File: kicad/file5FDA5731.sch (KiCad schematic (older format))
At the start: 14 parts, among them M1 BSC014N04LSI, M11 BSC014N04LSI, M12 BSC010N04LSI, M13 BSC015NE2LS5I, M14 BSC009NE2LS5I, M15 BSC014N04LSI, M17 BSC015NE2LS5I, M2 BSC010N04LSI, M3 BSC015NE2LS5I, M4 BSC009NE2LS5I, M5 BSC014N04LSI, M7 BSC015NE2LS5I

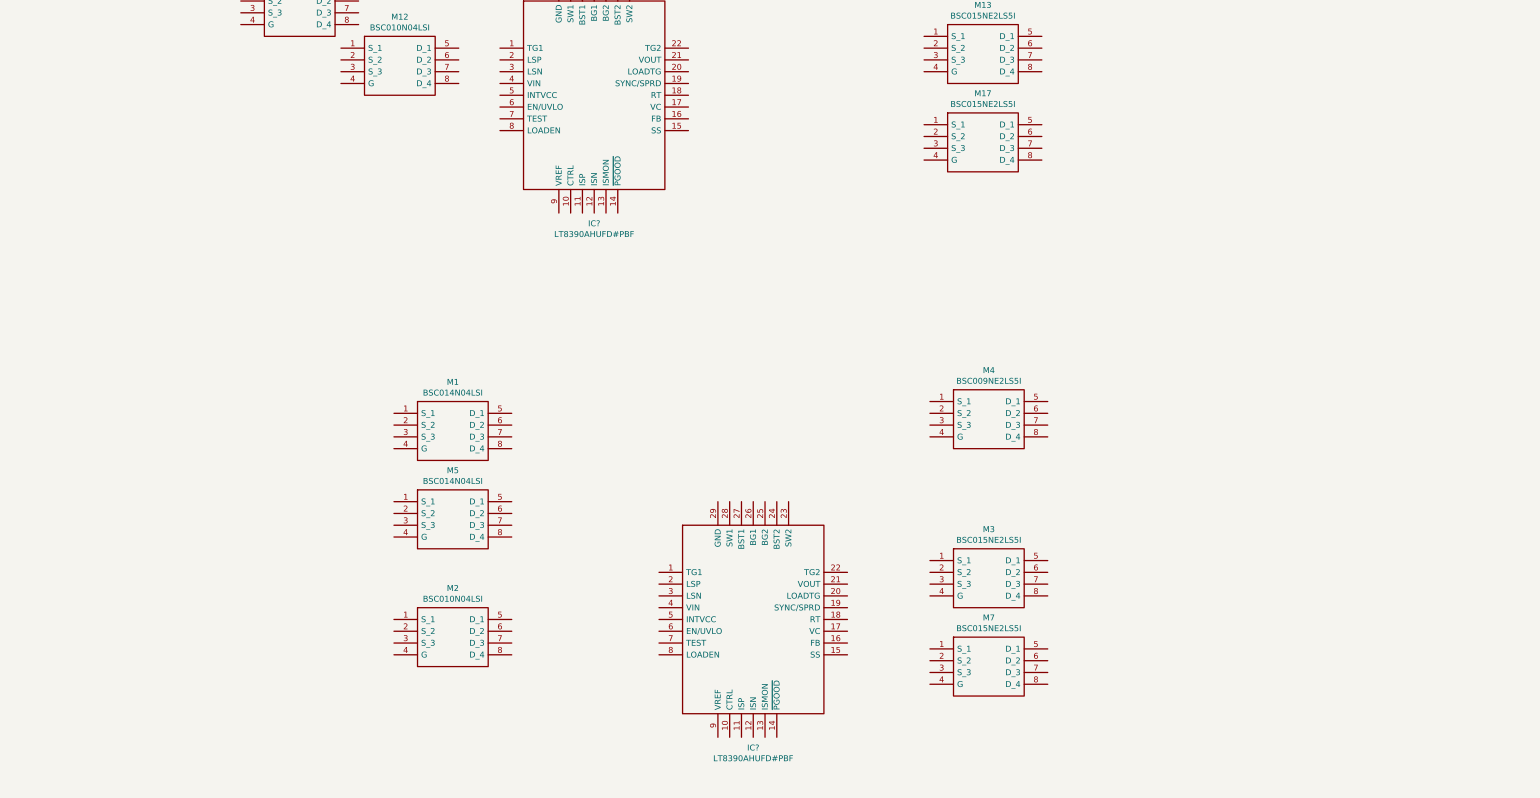
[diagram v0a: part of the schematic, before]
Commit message: Add Vin
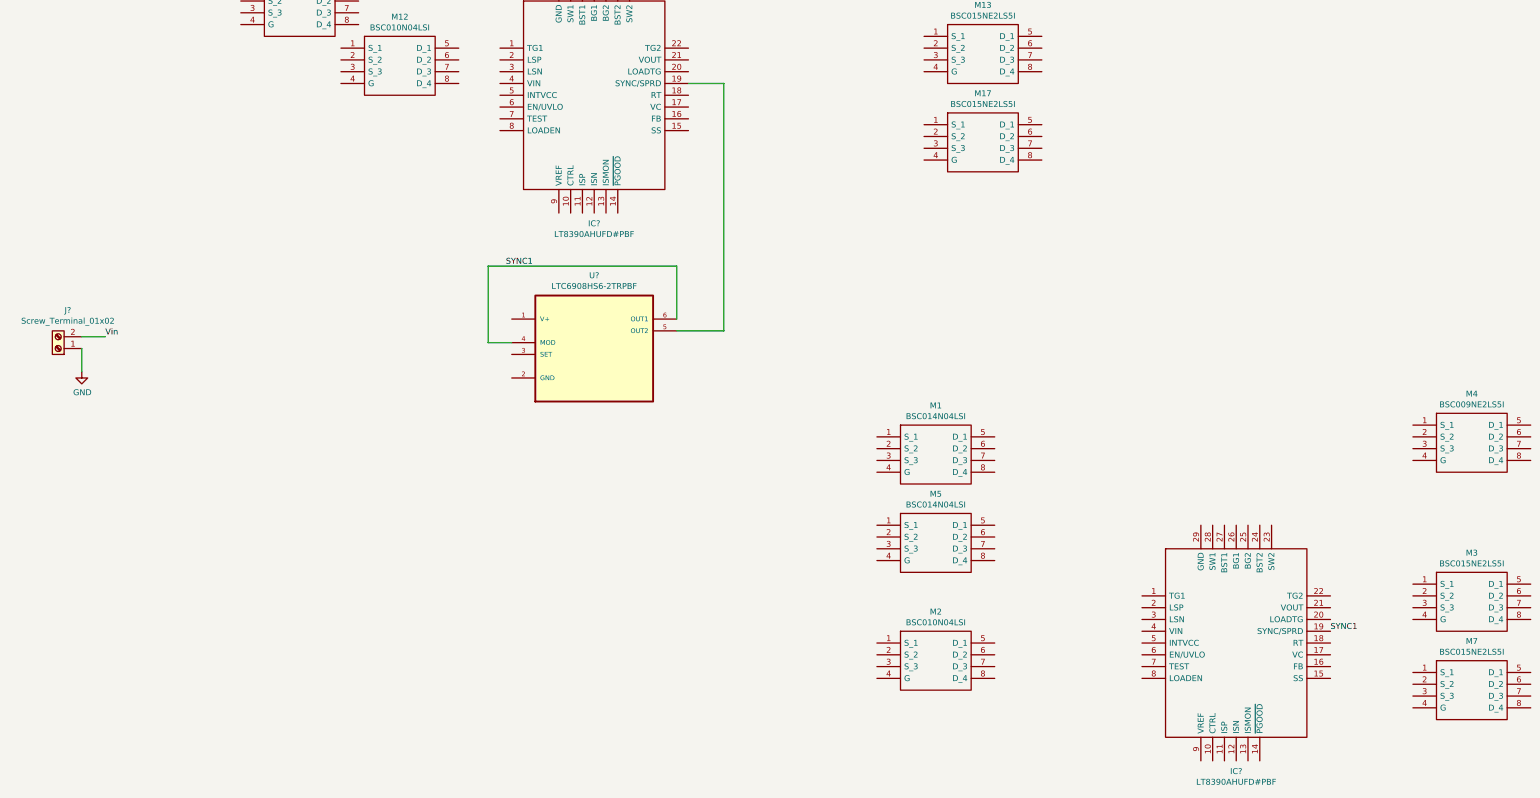
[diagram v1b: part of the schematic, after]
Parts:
- added J?: Screw_Terminal_01x02, symbol Connector:Screw_Terminal_01x02
- added U?: LTC6908HS6-2TRPBF, SOT95P280X100-6N, symbol LTC6908HS6-2TRPBF:LTC6908HS6-2TRPBF
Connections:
- net at IC?.19 (SYNC/SPRD): now also U?.5 (OUT2)
- net SYNC1: now reaches IC?.19 (SYNC/SPRD)
- net SYNC1: now also U?.4 (MOD), U?.6 (OUT1)
- new net GND: J?.1 (Pin_1)
- new net Vin: J?.2 (Pin_2)
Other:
- moved on the sheet: IC?, M1, M2, M3, M4, M5, M7

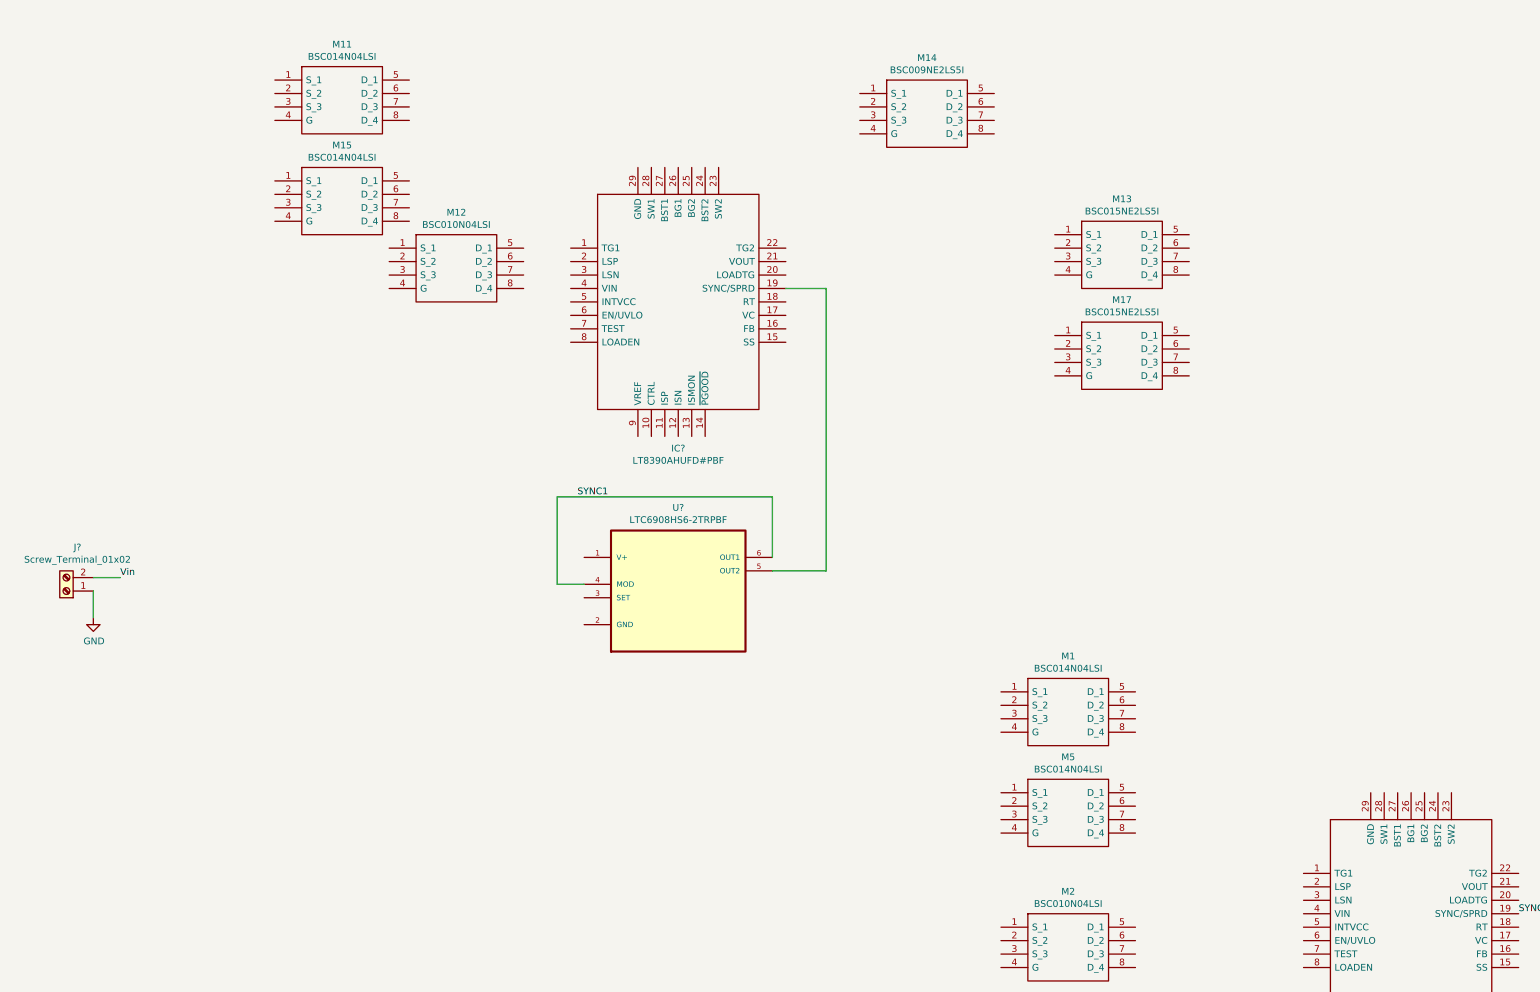
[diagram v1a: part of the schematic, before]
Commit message: Enter equipment power regulator schematic
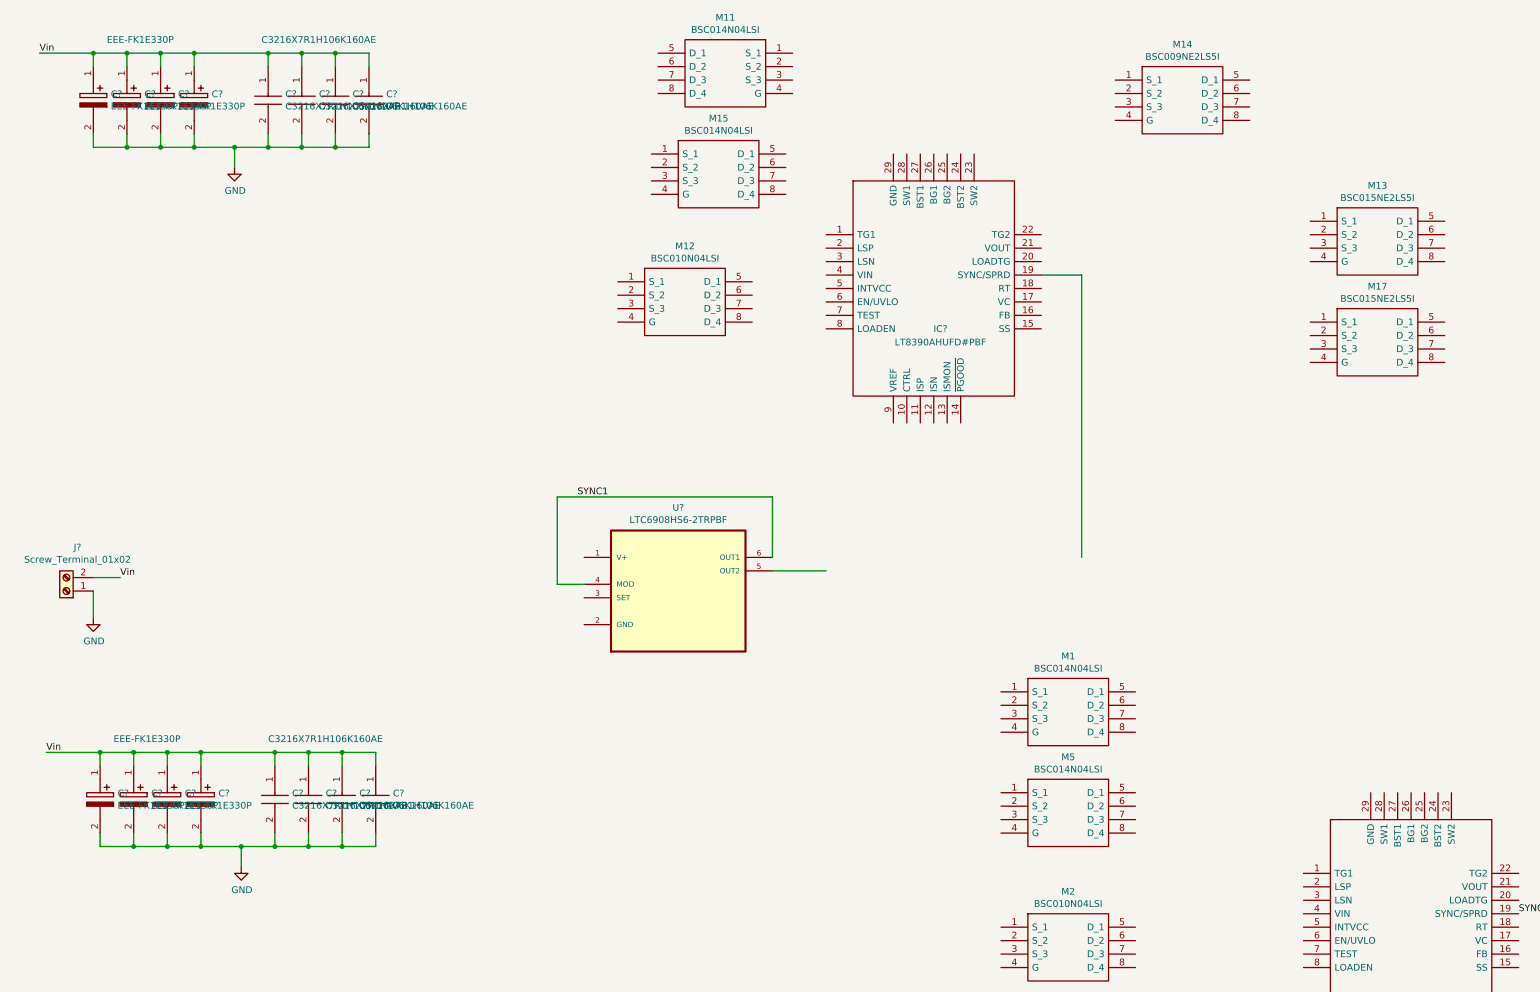
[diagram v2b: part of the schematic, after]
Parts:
- added C? (x8): C3216X7R1H106K160AE, CAPC3216X180N, symbol SamacSys_Parts:C3216X7R1H106K160AE
- added C? (x8): EEE-FK1E330P, CAPAE660X610N, symbol EEE-FK1E330P:EEE-FK1E330P
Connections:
- wire segments 9 -> 75
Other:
- moved on the sheet: IC?, M11, M12, M13, M14, M15, M17

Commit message: Power reg U2/U3 and supporting components
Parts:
- removed C? (x8): C3216X7R1H106K160AE, CAPC3216X180N, symbol SamacSys_Parts:C3216X7R1H106K160AE
- removed C? (x8): EEE-FK1E330P, CAPAE660X610N, symbol EEE-FK1E330P:EEE-FK1E330P
- removed IC?: LT8390AHUFD#PBF, QFN50P400X500X80-29N-D, symbol LT8390AHUFD#PBF:LT8390AHUFD#PBF
- removed M1, M5: BSC014N04LSI, BSC059N04LS6ATMA1, symbol BSC014N04LSI:BSC014N04LSI
- removed M2: BSC010N04LSI, TDSON-8FL, symbol BSC010N04LSI:BSC010N04LSI
- removed M3, M7: BSC015NE2LS5I, BSC059N04LS6ATMA1, symbol BSC014N04LSI:BSC014N04LSI
- removed M4: BSC009NE2LS5I, BSC059N04LS6ATMA1, symbol BSC014N04LSI:BSC014N04LSI
- added C32, C33, C34, C35: EEE-FK1E330P, CAPAE660X610N, symbol EEE-FK1E330P:EEE-FK1E330P
- added C36, C37, C38, C39: C3216X7R1H106K160AE, CAPC3216X180N, symbol SamacSys_Parts:C3216X7R1H106K160AE
- added C40, C42, C46, C54: 1uF, symbol Device:C_Small
- added C41: 0.47uF, symbol Device:C_Small
- added C43: 4.7uF, symbol Device:C_Small
- added C44, C47: 0.1uF, symbol Device:C_Small
- added C45: 3.3nF, symbol Device:C_Small
- added C48, C49, C50, C51: C3216X5R1C476M160AB, CAPC3216X180N, symbol SamacSys_Parts:C3216X5R1C476M160AB
- added C52, C53, C55, C56: 16SVF560M, CAPAE830X1200N, symbol SamacSys_Parts:16SVF560M
- added L3: B82559B2152A027, symbol Device:L
- added R11, R12: 100K, symbol Device:R_Small_US
- added R13, R14: KRL6432D-M-R002-G-T1, RESC3163X70N, symbol SamacSys_Parts:KRL6432E-M-R002-G-T1
- added R15: 3K, symbol Device:R_Small_US
- added R16: 309K, 150kHz, symbol Device:R_Small_US
- added R17: 665K, symbol Device:R_Small_US
- added R18, R19: KRL6432D-M-R006-G-T1, RESC3163X50N, symbol SamacSys_Parts:KRL6432E-C-R006-F-T1
- added R20, R21: 50, symbol Device:R_Small_US
- added R22: 604K, symbol Device:R_Small_US
- added R23: 49.9K, symbol Device:R_Small_US
- gave numbers to parts that had none: 3
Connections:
- net labels added: FB, ISMON, ISN, ISP, LSN, LSP, SYNC2, U2OUT, V+SET, VOUT
- wire segments 75 -> 261
- no-connect marks 0 -> 2
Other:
- note added: "150kHz CLOCK SOURCE\nWITH COMPLEMENTARY OUTPUTS"
- moved on the sheet: M11, M12, M13, M14, M15, M17, U3

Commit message: Cleanup power regulator Section 2
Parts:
- added C57: 1uF, symbol Device:C_Small
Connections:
- net FB is gone; now on net U2FB: R22.2, R23.1, U2.16 (FB)
- net V+SET is gone; now on net U2V+SET: U2.5 (INTVCC)
- net GND: now also C57.2; no longer C48.1, C49.1, C50.1, C51.1, C52.1, C53.1, M14.5 (D_1), M14.6 (D_2), M14.7 (D_3), M14.8 (D_4), R18.1, R19.1, R20.1, U2.21 (VOUT)
- net U2FB: now reaches C44.1, R11.1, U2.15 (SS)
- net U2SW2: now reaches C46.1, L3.2, M13.5 (D_1), M13.6 (D_2), M13.7 (D_3), M13.8 (D_4), M14.1 (S_1), M14.2 (S_2), M14.3 (S_3), M17.5 (D_1), M17.6 (D_2), M17.7 (D_3), M17.8 (D_4), U2.23 (SW2)
- net U2BG2: now reaches M17.4 (G), U2.25 (BG2)
- net U2BG1: now reaches M12.4 (G), U2.26 (BG1)
- net U2ENUVLO: now reaches U2.6 (EN/UVLO)
- net U2V+SET: now reaches C43.1, C47.1, R12.2, R17.1, U3.1 (V+)
- net ISMON renamed U2CTRL
- net ISN renamed U2ISN
- net ISP renamed U2ISP
- net LSN renamed U2LSN
- net LSP renamed U2LSP
- net SYNC1 renamed U3OUT1
- net SYNC2 renamed U2SYNC
- net U2OUT renamed Sec2VOUT
- new net U2VOUT: C48.1, C49.1, C50.1, C51.1, C52.1, C53.1, C57.1, M14.5 (D_1), M14.6 (D_2), M14.7 (D_3), M14.8 (D_4), R18.1, R19.1, R20.1, U2.21 (VOUT)
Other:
- moved on the sheet: C36, C37, C38, C39, C40, C41, C43, C44, C46, C47, J4, R11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

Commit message: Power regulator Section 2, 1st proofread
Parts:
- C42, C46: value 1uF -> 0.1uF
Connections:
- net U2FB: no longer C44.1, R11.1, U2.15 (SS)
- net U2V+SET renamed U2INTVCC
- new net: C44.1, R11.1, U2.15 (SS)
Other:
- note added: "Add jumper(s) so board can be used standalone."
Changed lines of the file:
@@
 P 9300 1300
 F 0 "C46" H 9392 1346 50  0000 L CNN
-F 1 "1uF" H 9392 1255 50  0000 L CNN
+F 1 "0.1uF" H 9392 1255 50  0000 L CNN
 F 2 "" H 9300 1300 50  0001 C CNN
 F 3 "~" H 9300 1300 50  0001 C CNN
@@
 P 7250 1350
 F 0 "C42" H 7342 1396 50  0000 L CNN
-F 1 "1uF" H 7342 1305 50  0000 L CNN
+F 1 "0.1uF" H 7342 1305 50  0000 L CNN
 F 2 "" H 7250 1350 50  0001 C CNN
 F 3 "~" H 7250 1350 50  0001 C CNN
@@
 Sec2VOUT
 Wire Wire Line
-	8300 3050 8300 3150
-Wire Wire Line
 	6150 2850 6550 2850
 Text Label 6150 2850 0    50   ~ 0
-U2V+SET
+U2INTVCC
 Text Label 7450 1800 1    50   ~ 0
 U2BG2
@@
 	7550 4800 7450 4800
 Text Label 7450 4800 2    50   ~ 0
-U2V+SET
+U2INTVCC
 Connection ~ 12400 1100
 Wire Wire Line
@@
 L power:GND #PWR012
 U 1 1 60DD625A
-P 8400 2250
-F 0 "#PWR012" H 8400 2000 50  0001 C CNN
-F 1 "GND" H 8405 2077 50  0000 C CNN
-F 2 "" H 8400 2250 50  0001 C CNN
-F 3 "" H 8400 2250 50  0001 C CNN
-	1    8400 2250
+P 8400 2300
+F 0 "#PWR012" H 8400 2050 50  0001 C CNN
+F 1 "GND" H 8405 2127 50  0000 C CNN
+F 2 "" H 8400 2300 50  0001 C CNN
+F 3 "" H 8400 2300 50  0001 C CNN
+	1    8400 2300
 	-1   0    0    1
 $EndComp
 Wire Wire Line
-	8400 2350 8400 2250
-Wire Wire Line
 	7050 1850 6900 1850
+Text Notes 1350 5850 0    197  ~ 0
+Add jumper(s) so board can be used standalone.
+Wire Wire Line
+	8400 2350 8400 2300
 $EndSCHEMATC

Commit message: Power reg Section 1 initial entry; annotate
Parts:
- added C58, C59, C60, C61: EEE-FK1E330P, CAPAE660X610N, symbol EEE-FK1E330P:EEE-FK1E330P
- added C62, C63, C64, C65: C3216X7R1H106K160AE, CAPC3216X180N, symbol SamacSys_Parts:C3216X7R1H106K160AE
- added C66, C70, C82: 1uF, symbol Device:C_Small
- added C67: 0.47uF, symbol Device:C_Small
- added C68, C71, C73: 0.1uF, symbol Device:C_Small
- added C69: 4.7uF, symbol Device:C_Small
- added C72: 47nF, symbol Device:C_Small
- added C74, C75, C76, C77: C3216X5R1C476M160AB, CAPC3216X180N, symbol SamacSys_Parts:C3216X5R1C476M160AB
- added C78, C79, C80, C81: 16SVF560M, CAPAE830X1200N, symbol SamacSys_Parts:16SVF560M
- added L4: B82559B2152A027, symbol Device:L
- added M1, M5: BSC014N04LSI, BSC059N04LS6ATMA1, symbol BSC014N04LSI:BSC014N04LSI
- added M2: BSC010N04LSI, TDSON-8FL, symbol BSC010N04LSI:BSC010N04LSI
- added M3, M7: BSC015NE2LS5I, BSC059N04LS6ATMA1, symbol BSC014N04LSI:BSC014N04LSI
- added M4: BSC009NE2LS5I, BSC059N04LS6ATMA1, symbol BSC014N04LSI:BSC014N04LSI
- added R24, R26: 365K, symbol Device:R_Small_US
- added R25, R27: 56.2K, symbol Device:R_Small_US
- added R28, R29, R30: 100K, symbol Device:R_Small_US
- added R31, R32: KRL6432D-M-R002-G-T1, RESC3163X70N, symbol SamacSys_Parts:KRL6432E-M-R002-G-T1
- added R33: 8.2K, symbol Device:R_Small_US
- added R34: 309K, 150kHz, symbol Device:R_Small_US
- added R35, R36: KRL6432D-M-R006-G-T1, RESC3163X50N, symbol SamacSys_Parts:KRL6432E-C-R006-F-T1
- added R37, R38: 15, symbol Device:R_Small_US
- added R39: 549K, symbol Device:R_Small_US
- added R40: 49.9K, symbol Device:R_Small_US
- added U1: LT8390AHUFD#PBF, QFN50P400X500X80-29N-D, symbol LT8390AHUFD#PBF:LT8390AHUFD#PBF
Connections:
- net GND: now also C58.2, C59.2, C60.2, C61.2, C62.2, C63.2, C64.2, C65.2, C66.2, C67.2, C69.2, C70.2, C71.2, C72.2, C74.2, C75.2, C76.2, C77.2, C78.2, C79.2, C80.2, C81.2, M2.1 (S_1), M2.2 (S_2), M2.3 (S_3), M3.1 (S_1), M3.2 (S_2), M3.3 (S_3), M3.4 (G), M7.1 (S_1), M7.2 (S_2), M7.3 (S_3), R25.2, R27.2, R28.2, R34.2, R40.2, U1.29 (GND), U1.7 (TEST)
- net U3OUT1: now also U1.19 (SYNC/SPRD)
- net Vin: now also C58.1, C59.1, C60.1, C61.1, C62.1, C63.1, C64.1, C65.1, C66.1, M1.5 (D_1), M1.6 (D_2), M1.7 (D_3), M1.8 (D_4), M5.5 (D_1), M5.6 (D_2), M5.7 (D_3), M5.8 (D_4), R24.1, R26.1, U1.4 (VIN)
- net Sec2VOUT renamed U1VOUT
- net U1VOUT: now also C70.1, C74.1, C75.1, C76.1, C77.1, C78.1, C79.1, C80.1, C81.1, M4.5 (D_1), M4.6 (D_2), M4.7 (D_3), M4.8 (D_4), R35.1, R36.1, R37.1, U1.21 (VOUT)
- net U2CTRL renamed U1ISMON
- net U1ISMON: now also R28.1, U1.13 (ISMON)
- net U2ENUVLO renamed ENUVLO
- net ENUVLO: now also R24.2, R25.1, R26.2, R27.1, U1.6 (EN/UVLO)
- new net: M1.4 (G), M5.4 (G), U1.1 (TG1)
- new net: C67.1, R29.2, U1.8 (LOADEN), U1.9 (VREF)
- new net: R30.1, U1.14 (~PGOOD)
- new net: R34.1, U1.18 (RT)
- new net: R33.1, U1.17 (VC)
- new net: C72.1, R33.2
- new net: C71.1, U1.15 (SS)
- new net: C73.2, U1.24 (BST2)
- new net: R29.1, U1.10 (CTRL)
- new net: M4.4 (G), U1.22 (TG2)
- new net: C68.2, U1.27 (BST1)
- new net PGOOD: C69.1, R30.2, U1.5 (INTVCC)
- new net U1BG1: M2.4 (G), U1.26 (BG1)
- new net U1BG2: M7.4 (G), U1.25 (BG2)
- new net U1FB: R39.2, R40.1, U1.16 (FB)
- new net U1ISN: C82.1, R38.2, U1.12 (ISN)
- new net U1ISP: C82.2, R37.2, U1.11 (ISP)
- new net U1LSN: L4.1, R31.2, R32.2, U1.3 (LSN)
- new net U1LSP: C68.1, M1.1 (S_1), M1.2 (S_2), M1.3 (S_3), M2.5 (D_1), M2.6 (D_2), M2.7 (D_3), M2.8 (D_4), M5.1 (S_1), M5.2 (S_2), M5.3 (S_3), R31.1, R32.1, U1.2 (LSP), U1.28 (SW1)
- new net U1SW2: C73.1, L4.2, M3.5 (D_1), M3.6 (D_2), M3.7 (D_3), M3.8 (D_4), M4.1 (S_1), M4.2 (S_2), M4.3 (S_3), M7.5 (D_1), M7.6 (D_2), M7.7 (D_3), M7.8 (D_4), U1.23 (SW2)
- new net VREG: R35.2, R36.2, R38.1, R39.1
- no-connect marks 2 -> 3
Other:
- note added: "13.8V (ADJ.)\n50A"
- note added: "Add jumper(s) to choose local enable or MCU-controlled enable so board can be used standalone."
- note removed: "Add jumper(s) so board can be used standalone."
